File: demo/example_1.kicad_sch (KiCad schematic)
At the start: 4 parts, among them U1 24C02

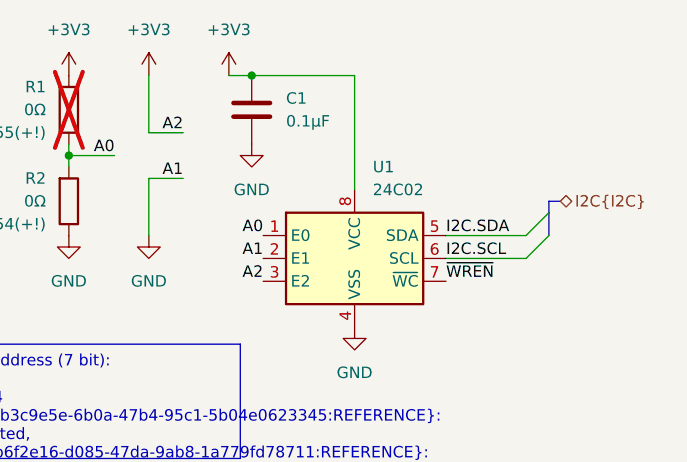
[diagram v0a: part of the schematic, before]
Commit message: Update demo project for upcoming changes
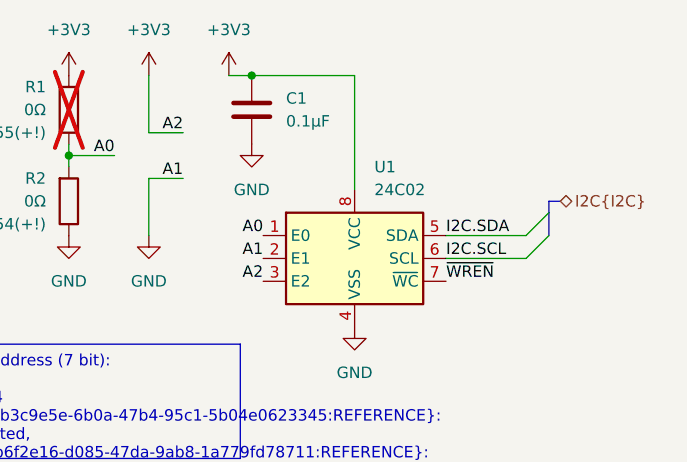
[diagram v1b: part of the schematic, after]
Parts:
- R1: KiVar.Rule EEPROM_ADDR 0x55(+!) -> (none); Var (none) -> EEPROM_ADDR 0x55(+!)
- R2: KiVar.Rule EEPROM_ADDR 0x54(+!) -> (none); Var (none) -> EEPROM_ADDR 0x54(+!)
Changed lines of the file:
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@@
 	(title_block
 		(title "KiVar Demo")
-		(date "2024-03-18")
+		(date "2024-03-19")
 		(company "Author: Mark Hämmerling <dev@markh.de>")
 		(comment 1 "https://github.com/markh-de/KiVar")
@@
 		(fields_autoplaced yes)
 		(property "Reference" "U1"
-			(at 131.5594 59.69 0)
+			(at 131.7341 59.69 0)
 			(effects
 				(font
@@
 		)
 		(property "Value" "24C02"
-			(at 131.5594 62.23 0)
+			(at 131.7341 62.23 0)
 			(effects
 				(font
@@
 			)
 		)
-		(property "KiVar.Rule" "EEPROM_ADDR 0x54(+!)"
+		(property "Var" "EEPROM_ADDR 0x54(+!)"
 			(at 95.25 66.0399 0)
 			(effects
@@
 			)
 		)
-		(property "KiVar.Rule" "EEPROM_ADDR 0x55(+!)"
+		(property "Var" "EEPROM_ADDR 0x55(+!)"
 			(at 95.25 55.8799 0)
 			(effects

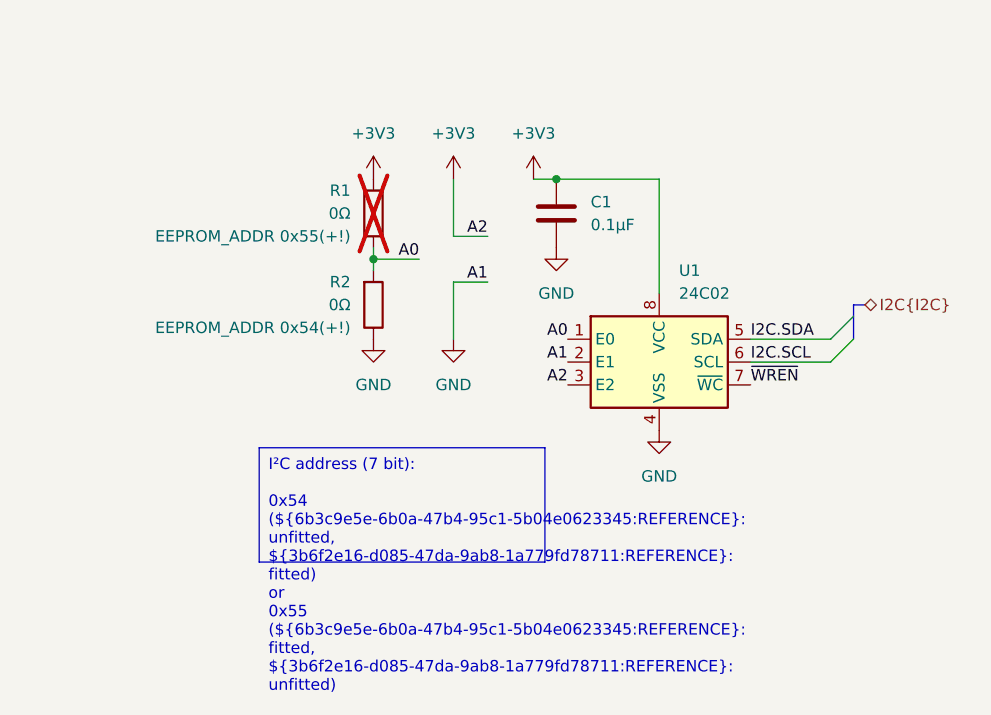
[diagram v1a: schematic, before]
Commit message: Make use of new 0.2.0 features in demo project, use different expression types
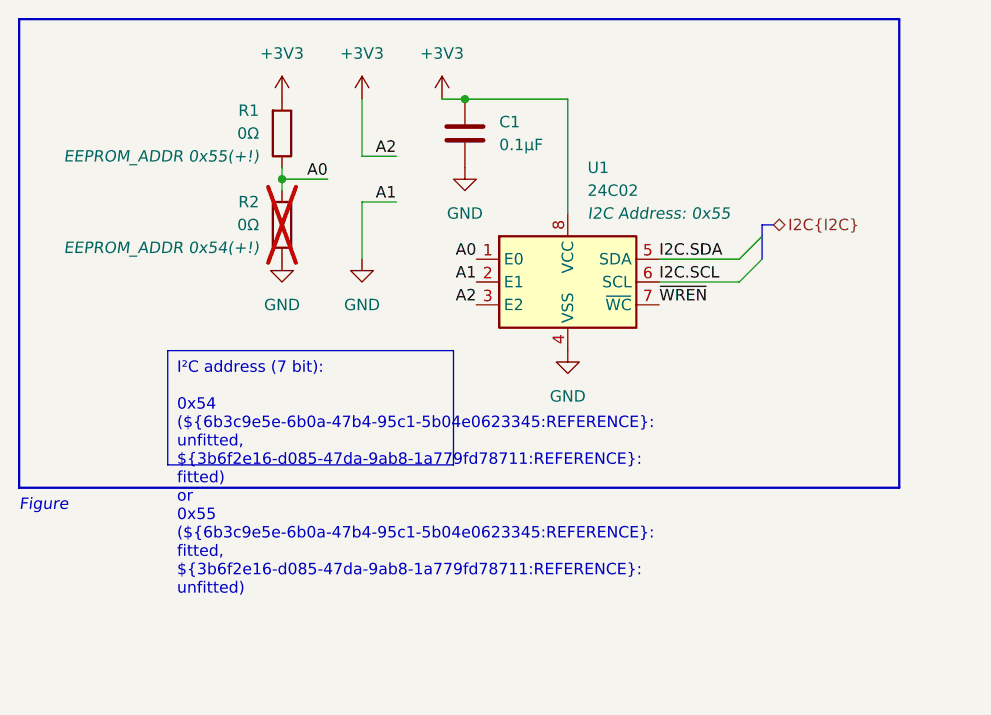
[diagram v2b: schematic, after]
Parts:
- R1: now fitted; now in the parts list
- R2: now not fitted; now left out of the parts list
- U1: I2C Address (none) -> 0x55; I2C Address.Var (none) -> 0x54(0x54) 0x55(0x55); Var (none) -> EEPROM_ADDR
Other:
- note added: "Figure"
- moved on the sheet: C1, U1
